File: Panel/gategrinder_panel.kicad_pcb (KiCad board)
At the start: 2 copper layers, 96 x 76 mm, 10 parts, among them J1 Conn_01x14, SW1 SW_SPST, SW2 SW_SPDT, SW3 SW_SPST, SW4 SW_SPDT

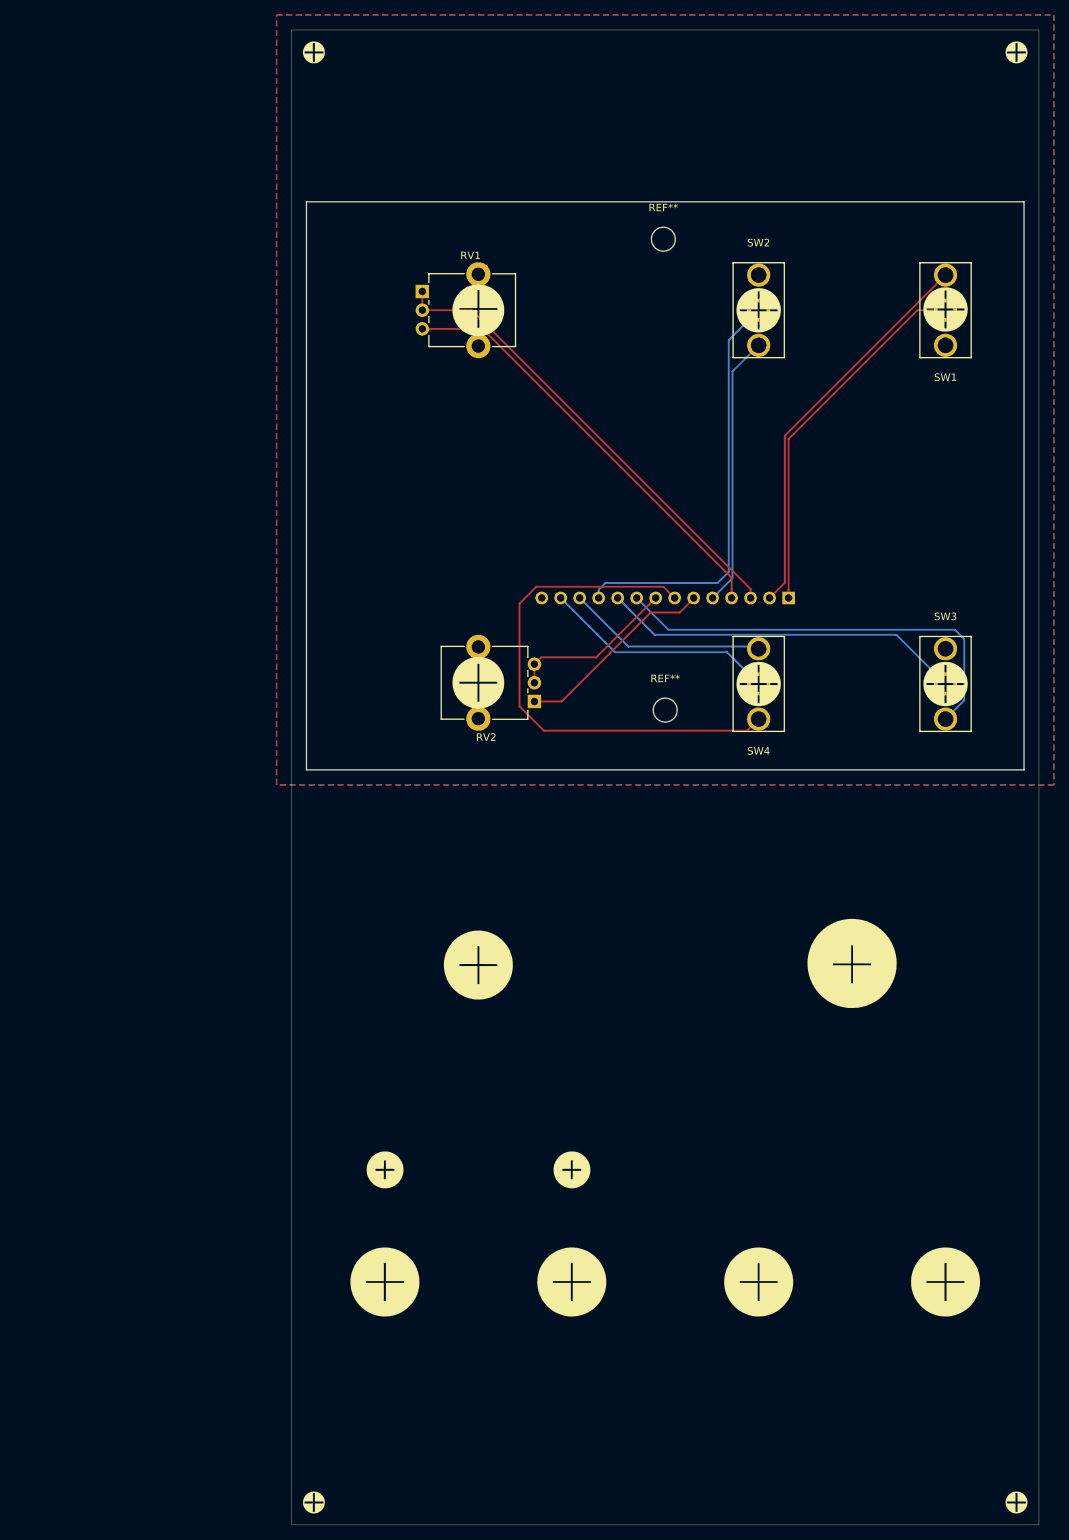
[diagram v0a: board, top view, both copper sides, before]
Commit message: Libraries cleanup and silkscreen work
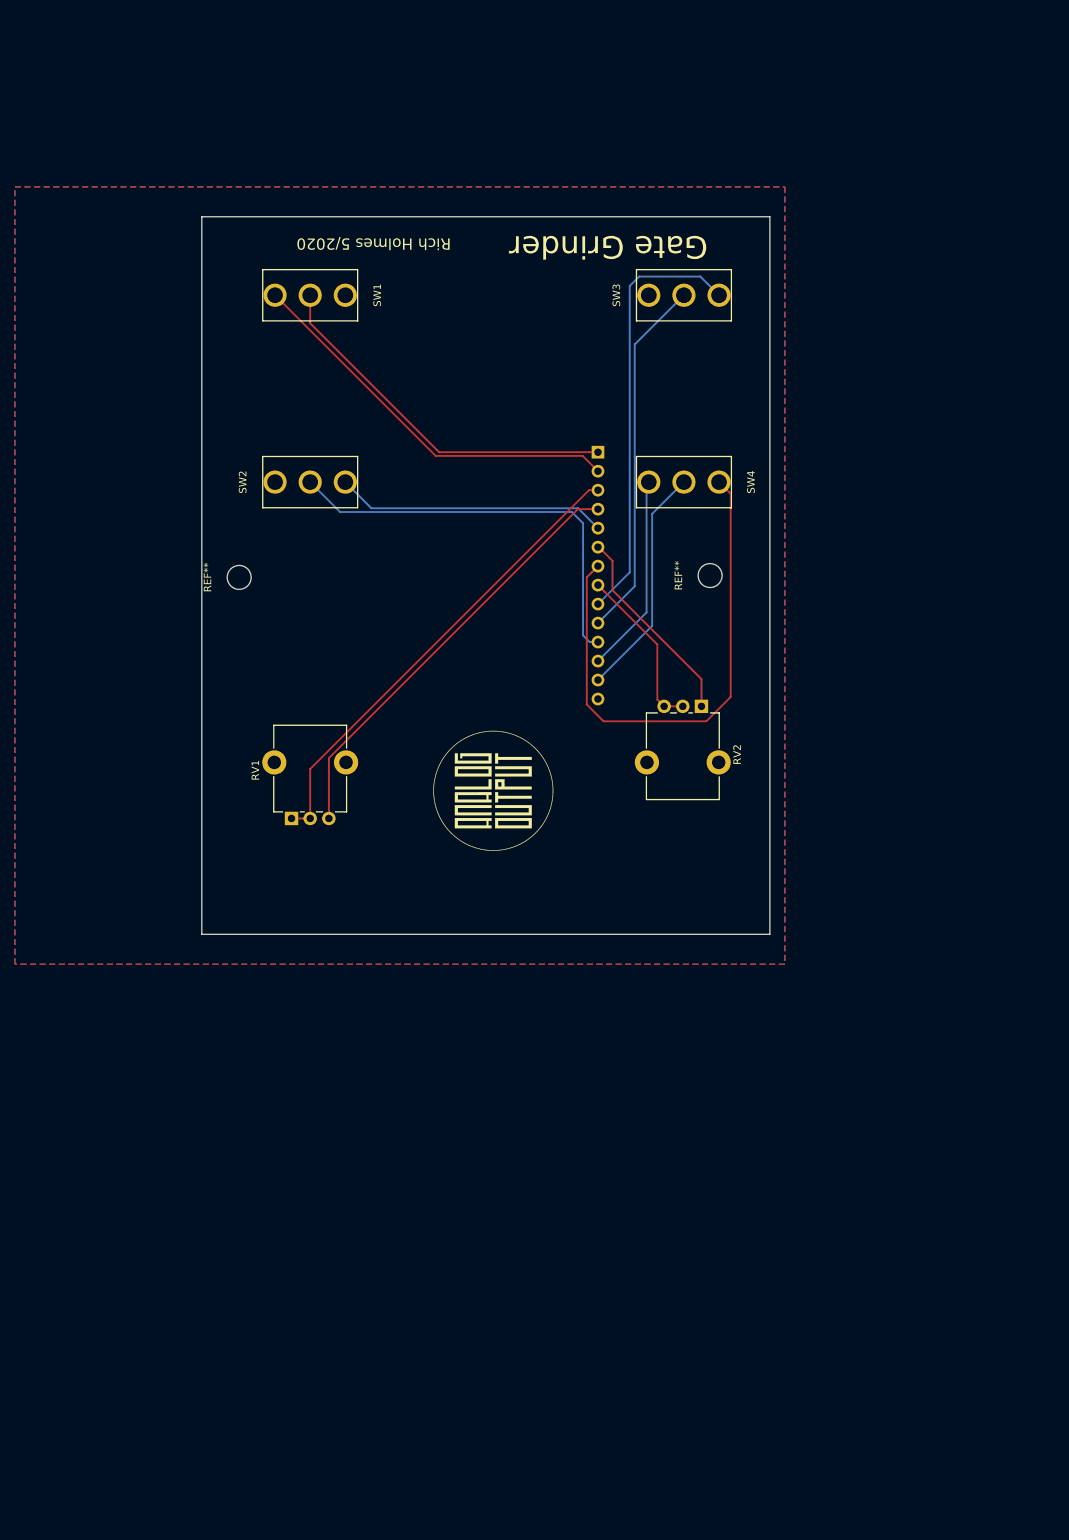
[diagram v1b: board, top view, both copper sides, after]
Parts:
- removed the G*** at (130.0, 119.0)
- added G***: LOGO, gategrinder_panel:analogoutput2, F.Cu at (107.0, 120.8)
- added G***: LOGO, gategrinder_panel:Gate_Grinder_panel_holes, F.Cu at (145.0, 92.0)
- moved SW1 85.0 mm to (82.5, 54.5), turned to 270 degrees
- moved RV1 72.6 mm to (80.0, 124.5), turned to 90 degrees
- moved REF** 72.6 mm to (73.0, 92.2), turned to 90 degrees
- moved SW2 64.3 mm to (82.5, 79.5), turned to 90 degrees
- moved SW3 62.7 mm to (132.5, 54.5), turned to 90 degrees
- moved J1 32.1 mm to (121.0, 75.5), turned to 180 degrees
- moved SW4 28.8 mm to (132.5, 79.5), turned to 270 degrees
- moved RV2 22.4 mm to (134.8, 109.5), turned to 270 degrees
- moved REF** 19.0 mm to (136.0, 92.0), turned to 90 degrees
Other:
- board size 96 x 76 mm -> 76 x 96 mm
- board text added: "Gate Grinder"
- board text added: "Rich Holmes 5/2020"
